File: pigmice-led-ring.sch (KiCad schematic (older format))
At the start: 51 parts, among them J1 Conn_01x02_Female, J2 Conn_01x03_Female, SW1 SW_Push, U1 LMR62014XMF

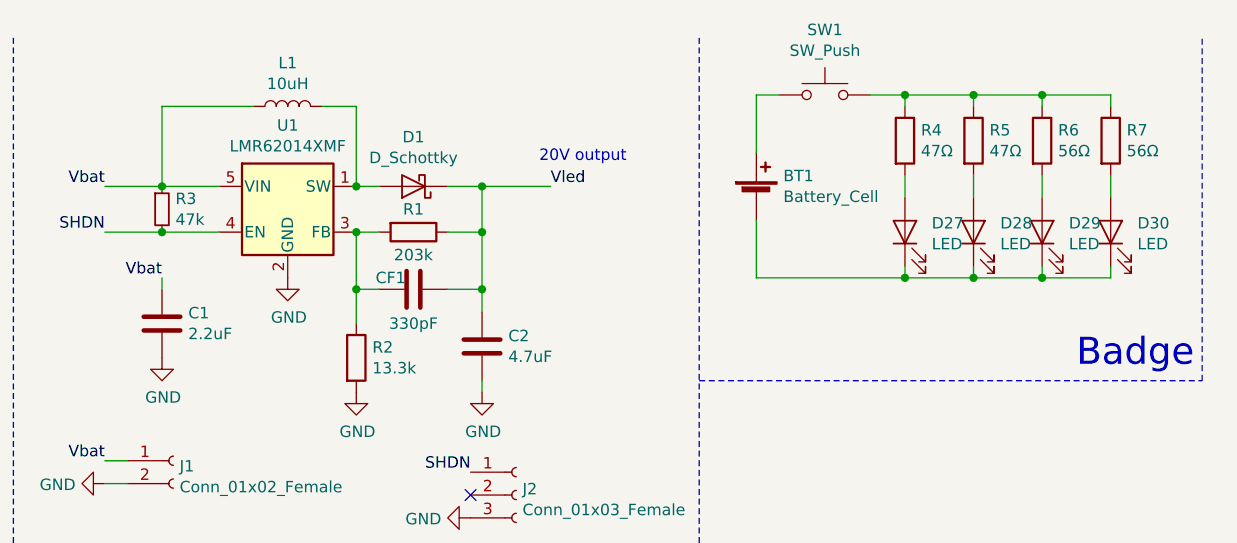
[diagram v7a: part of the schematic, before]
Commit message: Powerpole, DFM, optimize BOM
* Optimizes BOM to use cheaper components (~$15 components per board)
* Change power connector to use an Anderson connector
* Some DFM (remove copper fill logo, center part)
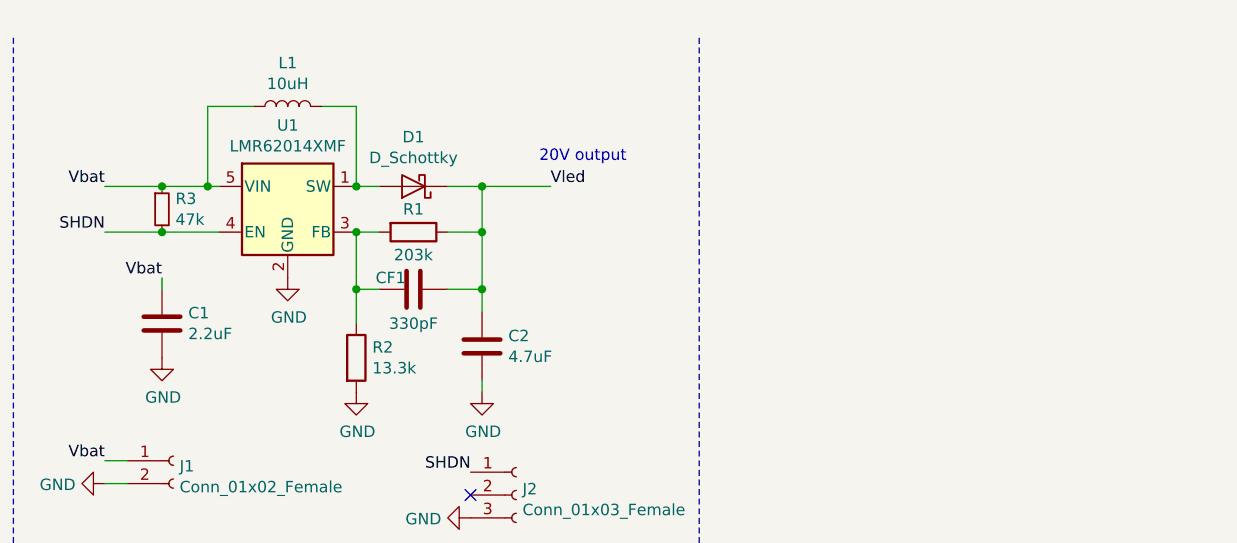
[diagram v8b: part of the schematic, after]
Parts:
- removed BT1: Battery_Cell, Battery:BatteryHolder_LINX_BAT-HLD-012-SMT, symbol Device:Battery_Cell
- removed D27, D28, D29, D30: LED, LED_SMD:LED_0603_1608Metric, symbol Device:LED
- removed R4, R5: 47Ω, Resistor_SMD:R_0603_1608Metric, symbol Device:R
- removed R6, R7: 56Ω, Resistor_SMD:R_0603_1608Metric, symbol Device:R
- removed SW1: SW_Push, Button_Switch_SMD:SW_SPST_B3U-1100P, symbol Switch:SW_Push
- J1: footprint Connector_Wire:SolderWirePad_1x02_P3.81mm_Drill1mm -> Connectors_Anderson:45A-VERT-PAIR
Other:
- note removed: "Badge"
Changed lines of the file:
@@
 $EndComp
-Wire Wire Line
-	1400 1150 1150 1150
 Wire Wire Line
 	1150 1350 1400 1350
@@
 	1    0    0    -1
 $EndComp
-$Comp
-L power:GND #PWR0101
-U 1 1 5E24B903
-P 1150 1900
-F 0 "#PWR0101" H 1150 1650 50  0001 C CNN
-F 1 "GND" H 1155 1727 50  0000 C CNN
-F 2 "" H 1150 1900 50  0001 C CNN
-F 3 "" H 1150 1900 50  0001 C CNN
-	1    1150 1900
-	1    0    0    -1
-$EndComp
-$Comp
-L Device:C C1
-U 1 1 5E1D1330
-P 1150 1750
-F 0 "C1" H 1265 1796 50  0000 L CNN
-F 1 "2.2uF" H 1265 1705 50  0000 L CNN
-F 2 "Capacitor_SMD:C_0805_2012Metric" H 1188 1600 50  0001 C CNN
-F 3 "~" H 1150 1750 50  0001 C CNN
-	1    1150 1750
-	1    0    0    -1
-$EndComp
-Wire Wire Line
-	1150 1550 1150 1600
-Text Label 1150 1550 2    50   ~ 0
-Vbat
 Connection ~ 2000 1150
 Wire Wire Line
 	2000 800  2000 1150
-Wire Wire Line
-	1150 800  1150 1150
-Connection ~ 1150 1150
-Wire Wire Line
-	900  1150 1150 1150
-Wire Wire Line
-	1550 800  1150 800
 NoConn ~ 2500 2500
 Text Label 2500 2400 2    50   ~ 0
@@
 F 0 "J1" H 1227 2326 50  0000 L CNN
 F 1 "Conn_01x02_Female" H 1227 2235 50  0000 L CNN
-F 2 "Connector_Wire:SolderWirePad_1x02_P3.81mm_Drill1mm" H 1200 2350 50  0001 C CNN
+F 2 "Connectors_Anderson:45A-VERT-PAIR" H 1200 2350 50  0001 C CNN
 F 3 "~" H 1200 2350 50  0001 C CNN
 	1    1200 2350
@@
 Text Notes 2600 5450 0    118  ~ 0
 LED Array
-$Comp
-L Device:LED D27
-U 1 1 5E2EAAA2
-P 4400 1350
-F 0 "D27" V 4439 1233 50  0000 R CNN
-F 1 "LED" V 4348 1233 50  0000 R CNN
-F 2 "LED_SMD:LED_0603_1608Metric" H 4400 1350 50  0001 C CNN
-F 3 "~" H 4400 1350 50  0001 C CNN
-	1    4400 1350
-	0    -1   -1   0
-$EndComp
-$Comp
-L Device:R R4
-U 1 1 5E2EEA86
-P 4400 950
-F 0 "R4" H 4470 996 50  0000 L CNN
-F 1 "47Ω" H 4470 905 50  0000 L CNN
-F 2 "Resistor_SMD:R_0603_1608Metric" V 4330 950 50  0001 C CNN
-F 3 "~" H 4400 950 50  0001 C CNN
-	1    4400 950
-	1    0    0    -1
-$EndComp
-$Comp
-L Device:R R5
-U 1 1 5E2EF046
-P 4700 950
-F 0 "R5" H 4770 996 50  0000 L CNN
-F 1 "47Ω" H 4770 905 50  0000 L CNN
-F 2 "Resistor_SMD:R_0603_1608Metric" V 4630 950 50  0001 C CNN
-F 3 "~" H 4700 950 50  0001 C CNN
-	1    4700 950
-	1    0    0    -1
-$EndComp
-$Comp
-L Device:LED D29
-U 1 1 5E2FBC97
-P 5000 1350
-F 0 "D29" V 5039 1233 50  0000 R CNN
-F 1 "LED" V 4948 1233 50  0000 R CNN
-F 2 "LED_SMD:LED_0603_1608Metric" H 5000 1350 50  0001 C CNN
-F 3 "~" H 5000 1350 50  0001 C CNN
-	1    5000 1350
-	0    -1   -1   0
-$EndComp
-$Comp
-L Device:LED D30
-U 1 1 5E2FBC9D
-P 5300 1350
-F 0 "D30" V 5339 1233 50  0000 R CNN
-F 1 "LED" V 5248 1233 50  0000 R CNN
-F 2 "LED_SMD:LED_0603_1608Metric" H 5300 1350 50  0001 C CNN
-F 3 "~" H 5300 1350 50  0001 C CNN
-	1    5300 1350
-	0    -1   -1   0
-$EndComp
-$Comp
-L Device:R R6
-U 1 1 5E2FBCA3
-P 5000 950
-F 0 "R6" H 5070 996 50  0000 L CNN
-F 1 "56Ω" H 5070 905 50  0000 L CNN
-F 2 "Resistor_SMD:R_0603_1608Metric" V 4930 950 50  0001 C CNN
-F 3 "~" H 5000 950 50  0001 C CNN
-	1    5000 950
-	1    0    0    -1
-$EndComp
-$Comp
-L Device:R R7
-U 1 1 5E2FBCA9
-P 5300 950
-F 0 "R7" H 5370 996 50  0000 L CNN
-F 1 "56Ω" H 5370 905 50  0000 L CNN
-F 2 "Resistor_SMD:R_0603_1608Metric" V 5230 950 50  0001 C CNN
-F 3 "~" H 5300 950 50  0001 C CNN
-	1    5300 950
-	1    0    0    -1
-$EndComp
-$Comp
-L Device:Battery_Cell BT1
-U 1 1 5E2E9E0D
-P 3750 1200
-F 0 "BT1" H 3868 1296 50  0000 L CNN
-F 1 "Battery_Cell" H 3868 1205 50  0000 L CNN
-F 2 "Battery:BatteryHolder_LINX_BAT-HLD-012-SMT" V 3750 1260 50  0001 C CNN
-F 3 "~" V 3750 1260 50  0001 C CNN
-	1    3750 1200
-	1    0    0    -1
-$EndComp
-Wire Wire Line
-	4400 1100 4400 1200
-Wire Wire Line
-	4700 1100 4700 1200
-Wire Wire Line
-	5000 1100 5000 1200
-Wire Wire Line
-	5300 1100 5300 1200
-Wire Notes Line
-	3500 2000 5700 2000
-Wire Notes Line
-	5700 2000 5700 500
-Text Notes 5150 1950 0    118  ~ 0
-Badge
-Wire Wire Line
-	4400 750  4400 800
-Wire Wire Line
-	4400 750  4700 750
-Wire Wire Line
-	4700 750  4700 800
-Wire Wire Line
-	4700 750  5000 750
-Wire Wire Line
-	5000 750  5000 800
-Connection ~ 4700 750
-Wire Wire Line
-	5000 750  5300 750
-Wire Wire Line
-	5300 750  5300 800
-Connection ~ 5000 750
-$Comp
-L Device:LED D28
-U 1 1 5E2EB354
-P 4700 1350
-F 0 "D28" V 4739 1233 50  0000 R CNN
-F 1 "LED" V 4648 1233 50  0000 R CNN
-F 2 "LED_SMD:LED_0603_1608Metric" H 4700 1350 50  0001 C CNN
-F 3 "~" H 4700 1350 50  0001 C CNN
-	1    4700 1350
-	0    -1   -1   0
-$EndComp
-Wire Wire Line
-	3750 1550 4400 1550
-Wire Wire Line
-	4400 1550 4400 1500
-Wire Wire Line
-	4400 1550 4700 1550
-Wire Wire Line
-	4700 1550 4700 1500
-Connection ~ 4400 1550
-Wire Wire Line
-	4700 1550 5000 1550
-Wire Wire Line
-	5000 1550 5000 1500
-Connection ~ 4700 1550
-Wire Wire Line
-	5000 1550 5300 1550
-Wire Wire Line
-	5300 1550 5300 1500
-Connection ~ 5000 1550
-$Comp
-L Switch:SW_Push SW1
-U 1 1 5E2C1562
-P 4050 750
-F 0 "SW1" H 4050 1035 50  0000 C CNN
-F 1 "SW_Push" H 4050 944 50  0000 C CNN
-F 2 "Button_Switch_SMD:SW_SPST_B3U-1100P" H 4050 950 50  0001 C CNN
-F 3 "~" H 4050 950 50  0001 C CNN
-	1    4050 750
-	1    0    0    -1
-$EndComp
-Wire Wire Line
-	3750 1550 3750 1300
-Wire Wire Line
-	3750 750  3850 750
-Wire Wire Line
-	3750 750  3750 1000
-Wire Wire Line
-	4250 750  4400 750
-Connection ~ 4400 750
+Connection ~ 1150 1150
+Wire Wire Line
+	900  1150 1150 1150
+Wire Wire Line
+	1150 1550 1150 1600
+$Comp
+L Device:C C1
+U 1 1 5E1D1330
+P 1150 1750
+F 0 "C1" H 1265 1796 50  0000 L CNN
+F 1 "2.2uF" H 1265 1705 50  0000 L CNN
+F 2 "Capacitor_SMD:C_0805_2012Metric" H 1188 1600 50  0001 C CNN
+F 3 "~" H 1150 1750 50  0001 C CNN
+	1    1150 1750
+	1    0    0    -1
+$EndComp
+$Comp
+L power:GND #PWR0101
+U 1 1 5E24B903
+P 1150 1900
+F 0 "#PWR0101" H 1150 1650 50  0001 C CNN
+F 1 "GND" H 1155 1727 50  0000 C CNN
+F 2 "" H 1150 1900 50  0001 C CNN
+F 3 "" H 1150 1900 50  0001 C CNN
+	1    1150 1900
+	1    0    0    -1
+$EndComp
+Text Label 1150 1550 2    50   ~ 0
+Vbat
+Wire Wire Line
+	1350 1150 1350 800
+Wire Wire Line
+	1350 800  1550 800
+Wire Wire Line
+	1150 1150 1350 1150
+Wire Wire Line
+	1350 1150 1400 1150
+Connection ~ 1350 1150
 $EndSCHEMATC
